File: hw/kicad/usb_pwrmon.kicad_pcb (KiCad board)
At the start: 2 copper layers, 23.9 x 17.5 mm, 15 parts, among them J1 16_PIN_HDR, J2 OLED_FPC_CONN

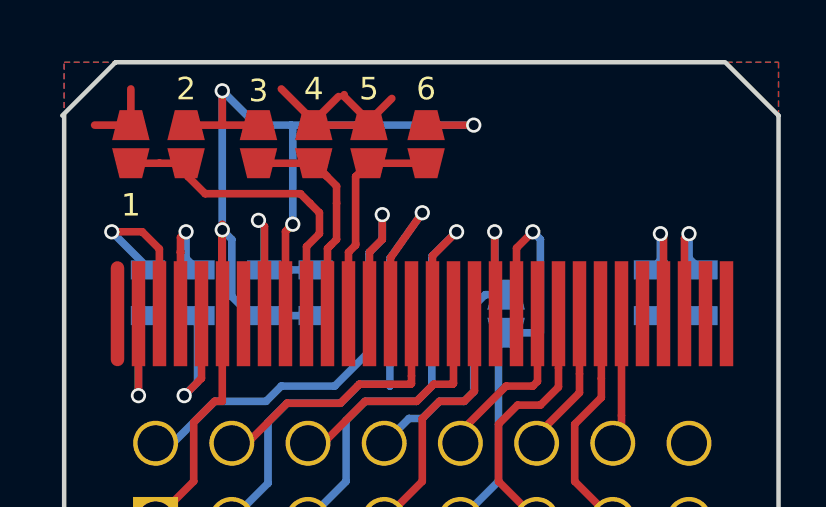
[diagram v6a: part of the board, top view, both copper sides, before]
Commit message: - forgot to add footprint for r1
Former-commit-id: 6fa6338699d94fe8eb54d1dcac4f5338db877c7e [formerly 6fa6338699d94fe8eb54d1dcac4f5338db877c7e [formerly 8823c0cdd6673d26dffb1b901427ca3f110487d3]]
Former-commit-id: f6e8cf4ef06b1c32549699c35b10a2e7af572ef4
Former-commit-id: e190ec155fe0a6c2ccca85e1ced67a6d5495672b
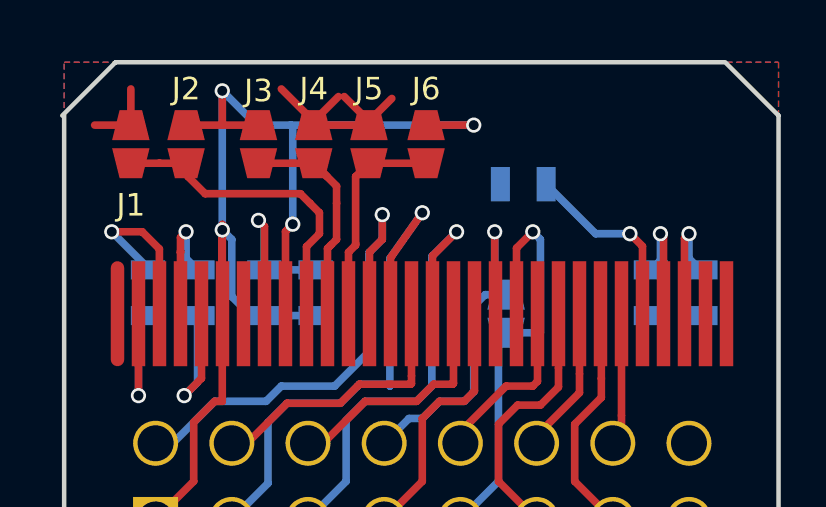
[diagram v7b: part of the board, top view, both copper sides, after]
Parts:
- added R1: 390R, SM0603, B.Cu at (158.3, 84.7)
- renumbered 1 to J1, 2 to J2, 3 to J3, 4 to J4, 5 to J5, 6 to J6
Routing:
- net N-000002: track 0.00 -> 6.32 mm, vias 0 -> 1
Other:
- board text added: "git.io/18upyg oled_brkout v0.2"
- board text removed: "git.io/18upyg oled_brkout v0.1"
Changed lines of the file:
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@@
 (kicad_pcb (version 3) (host pcbnew "(2013-07-07 BZR 4022)-stable")
   (general
-    (links 46)
+    (links 48)
     (no_connects 0)
-    (area 139.044334 80.569999 167.098405 98.484)
+    (area 142.863499 80.569999 166.889501 98.246001)
     (thickness 1.6)
     (drawings 9)
-    (tracks 214)
+    (tracks 218)
     (zones 0)
-    (modules 15)
+    (modules 16)
     (nets 26)
   )
@@
   (module jmp_small (layer F.Cu)
     (at 147.066 83.3755 180)
-    (fp_text reference 2 (at 0 1.8415 180) (layer F.SilkS)
+    (fp_text reference J2 (at 0 1.8415 180) (layer F.SilkS)
       (effects (font (size 0.75 0.75) (thickness 0.13)))
     )
@@
   (module jmp_small (layer F.Cu)
     (at 155.067 83.3755 180)
-    (fp_text reference 6 (at 0 1.8415 180) (layer F.SilkS)
+    (fp_text reference J6 (at 0 1.8415 180) (layer F.SilkS)
       (effects (font (size 0.75 0.75) (thickness 0.13)))
     )
@@
   (module jmp_small (layer F.Cu)
     (at 149.479 83.3755 180)
-    (fp_text reference 3 (at 0 1.778 180) (layer F.SilkS)
+    (fp_text reference J3 (at 0 1.778 180) (layer F.SilkS)
       (effects (font (size 0.75 0.75) (thickness 0.13)))
     )
@@
   (module jmp_small (layer F.Cu)
     (at 145.2245 83.3755 180)
-    (fp_text reference 1 (at 0 -2.032 180) (layer F.SilkS)
+    (fp_text reference J1 (at 0 -2.032 180) (layer F.SilkS)
       (effects (font (size 0.75 0.75) (thickness 0.13)))
     )
@@
   (module jmp_small (layer F.Cu)
     (at 151.3205 83.3755 180)
-    (fp_text reference 4 (at 0 1.8415 180) (layer F.SilkS)
+    (fp_text reference J4 (at 0 1.8415 180) (layer F.SilkS)
       (effects (font (size 0.75 0.75) (thickness 0.13)))
     )
@@
   (module jmp_small (layer F.Cu)
     (at 153.162 83.3755 180)
-    (fp_text reference 5 (at 0 1.8415 180) (layer F.SilkS)
+    (fp_text reference J5 (at 0 1.8415 180) (layer F.SilkS)
       (effects (font (size 0.75 0.75) (thickness 0.13)))
     )
@@
     )
   )
-  (gr_text "git.io/18upyg\noled_brkout\nv0.1" (at 161.798 82.296) (layer B.Mask)
+  (module SM0603 (layer B.Cu)
+    (at 158.3055 84.709)
+    (attr smd)
+    (fp_text reference R1 (at 0 0) (layer B.SilkS)
+      (effects (font (size 0.508 0.4572) (thickness 0.1143)) (justify mirror))
+    )
+    (fp_text value 390R (at 0 0) (layer B.SilkS) hide
+      (effects (font (size 0.508 0.4572) (thickness 0.1143)) (justify mirror))
+    )
+    (fp_line (start -1.143 0.635) (end 1.143 0.635) (layer B.SilkS) (width 0.127))
+    (fp_line (start 1.143 0.635) (end 1.143 -0.635) (layer B.SilkS) (width 0.127))
+    (fp_line (start 1.143 -0.635) (end -1.143 -0.635) (layer B.SilkS) (width 0.127))
+    (fp_line (start -1.143 -0.635) (end -1.143 0.635) (layer B.SilkS) (width 0.127))
+    (pad 1 smd rect (at -0.762 0) (size 0.635 1.143)
+      (layers B.Cu B.Paste B.Mask)
+      (net 15 GND)
+    )
+    (pad 2 smd rect (at 0.762 0) (size 0.635 1.143)
+      (layers B.Cu B.Paste B.Mask)
+      (net 20 N-000002)
+    )
+    (model smd\resistors\R0603.wrl
+      (at (xyz 0 0 0.001))
+      (scale (xyz 0.5 0.5 0.5))
+      (rotate (xyz 0 0 0))
+    )
+  )
+  (gr_text "git.io/18upyg\noled_brkout\nv0.2" (at 161.29 81.7245) (layer B.Mask)
     (effects (font (size 0.75 0.75) (thickness 0.13)) (justify mirror))
   )
@@
   (segment (start 153.162 82.7405) (end 153.162 82.6135) (width 0.254) (layer F.Cu) (net 15))
   (segment (start 153.162 82.6135) (end 153.924 81.8515) (width 0.254) (layer F.Cu) (net 15))
-  (segment (start 152.3365 81.788) (end 152.3365 81.7245) (width 0.254) (layer F.Cu) (net 15))
   (segment (start 153.162 82.6135) (end 152.3365 81.788) (width 0.254) (layer F.Cu) (net 15))
   (segment (start 151.3205 82.7405) (end 151.3205 82.6135) (width 0.254) (layer F.Cu) (net 15))
@@
   (segment (start 147.447 89.0905) (end 147.447 91.313) (width 0.254) (layer B.Cu) (net 19))
   (segment (start 147.58 91.18) (end 147.58 89.027) (width 0.254) (layer F.Cu) (net 19))
+  (segment (start 162.28 89.027) (end 162.28 86.7785) (width 0.254) (layer F.Cu) (net 20))
+  (segment (start 160.7185 86.36) (end 159.0675 84.709) (width 0.254) (layer B.Cu) (net 20))
+  (segment (start 161.8615 86.36) (end 160.7185 86.36) (width 0.254) (layer B.Cu) (net 20))
+  (via (at 161.8615 86.36) (size 0.508) (drill 0.33) (layers F.Cu B.Cu) (net 20))
+  (segment (start 162.28 86.7785) (end 161.8615 86.36) (width 0.254) (layer F.Cu) (net 20))
   (segment (start 162.8775 87.249) (end 162.56 87.5665) (width 0.254) (layer B.Cu) (net 21))
   (segment (start 162.8775 86.36) (end 162.8775 87.249) (width 0.254) (layer B.Cu) (net 21))
